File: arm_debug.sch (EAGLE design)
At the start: 14 parts, among them P1 FTSH-105-01-L-DV-K-TR, P2 FTSH-105-01-L-DV-K-TR, P3 MOLEX_MICRO_USB, P4 MEC6-110-02-L-D-RA1, U1 FT234XD-T

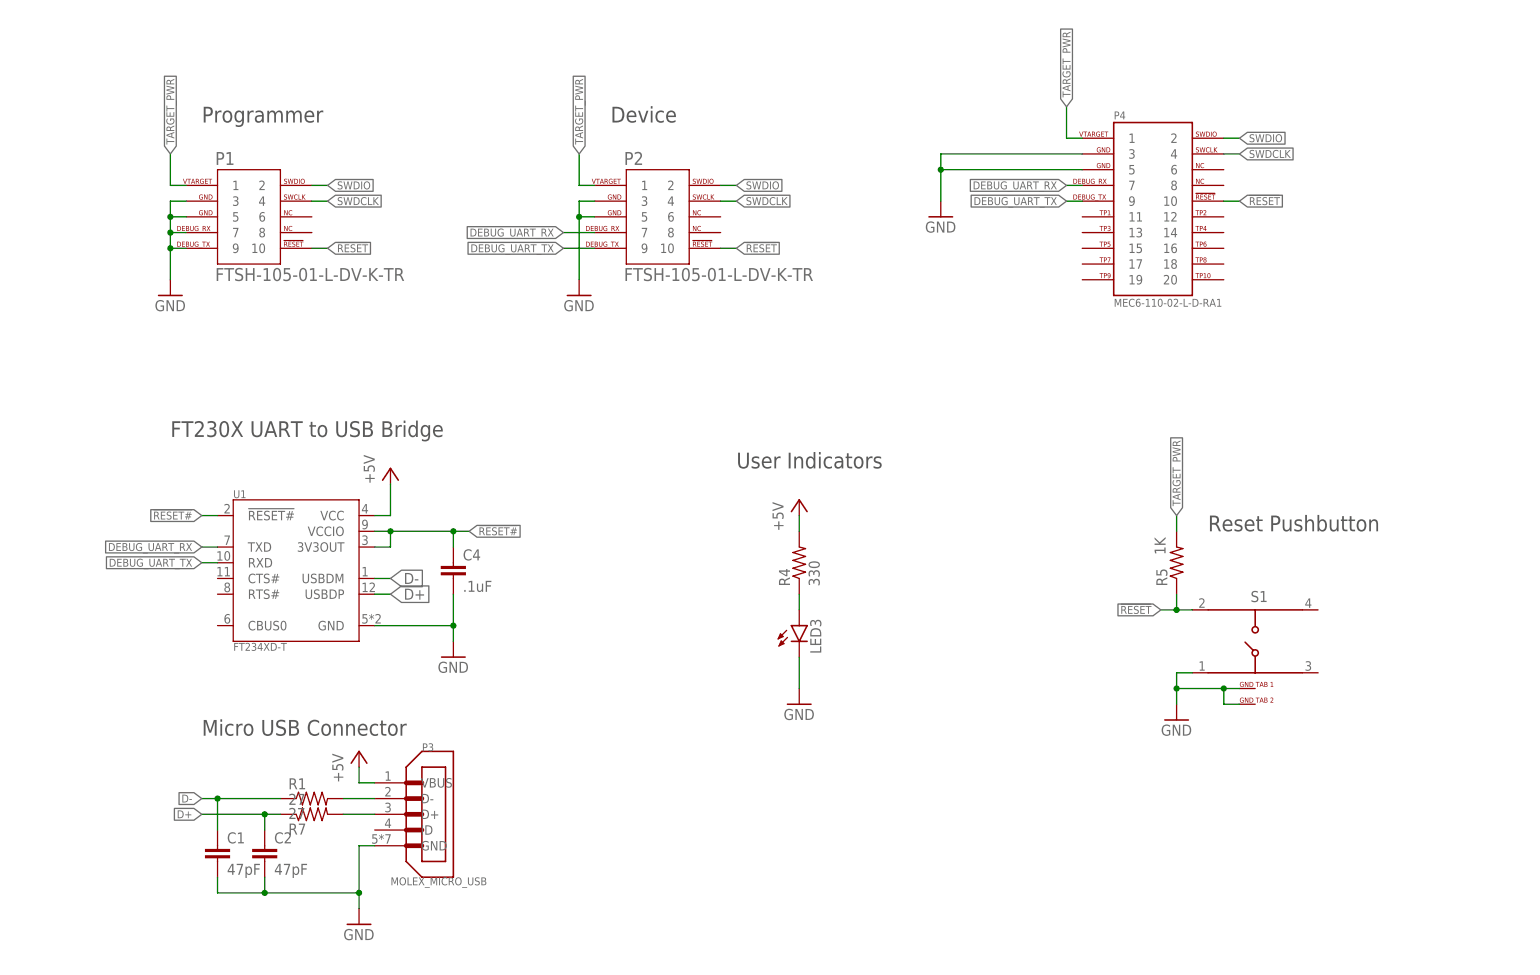
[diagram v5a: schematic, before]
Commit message: Seperating passive components into individual managed libraries
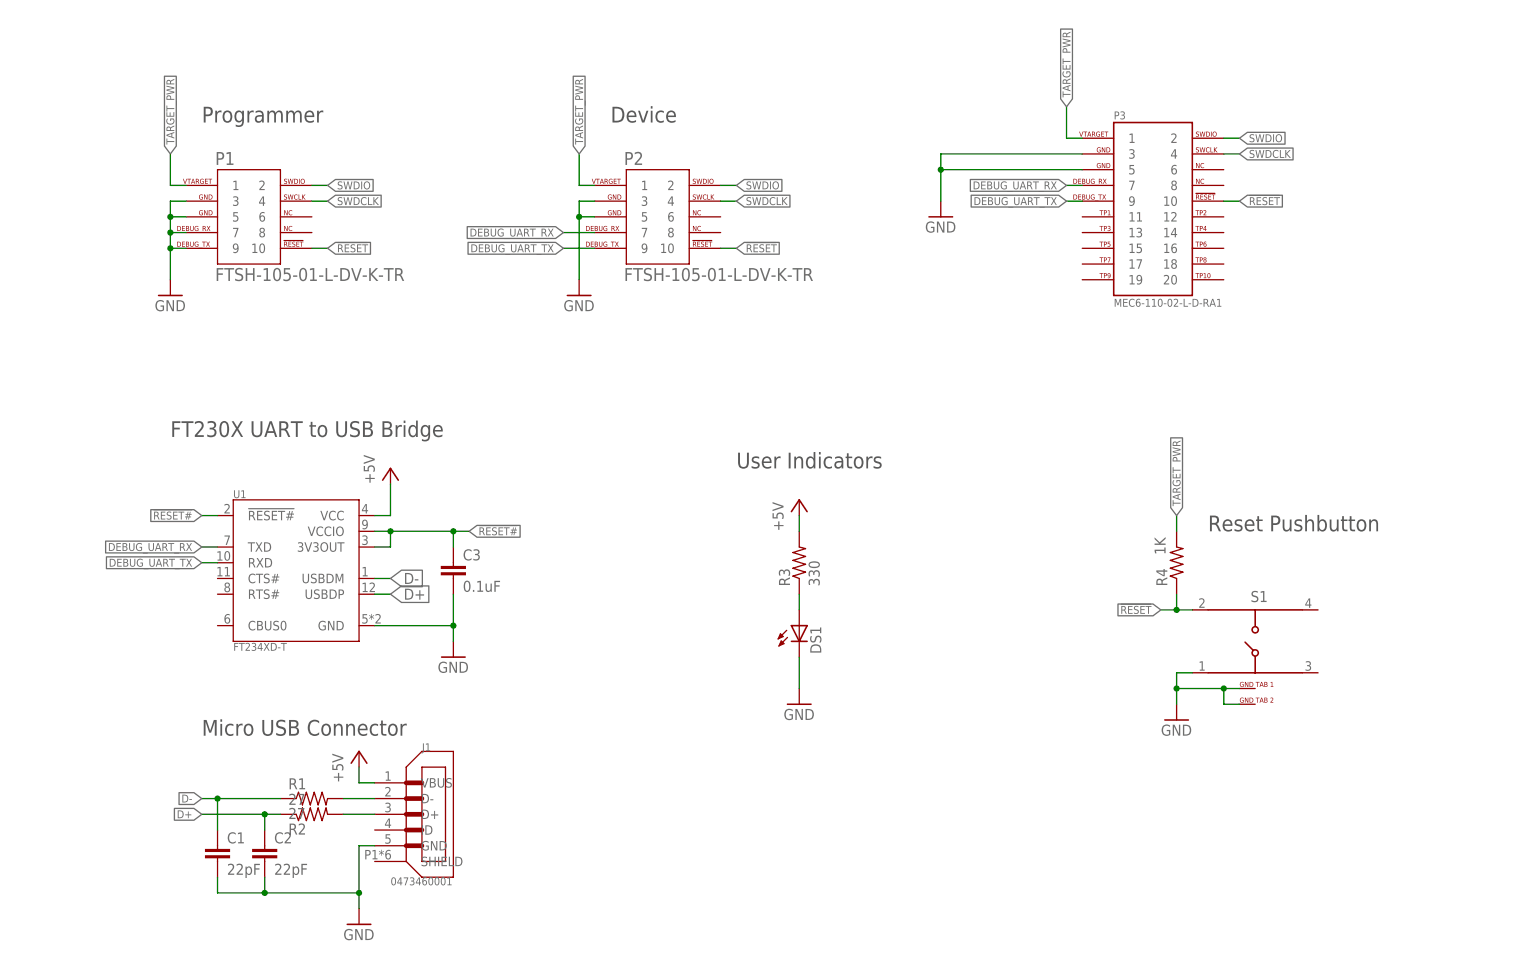
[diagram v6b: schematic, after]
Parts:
- removed C4: .1uF, resistor:C-EUC0603
- removed LED3: (no value), led:LEDCHIPLED_0603
- removed P4: MEC6-110-02-L-D-RA1, programming_headers:SWD-MEC10-F
- removed R5: 1K, resistor:R-US_R0603
- removed R7: 27, resistor:R-US_R0603
- added C3: 0.1uF, capacitors:0603YC104KAT2A
- added DS1: (no value), leds:LED0603
- added J1: 0473460001, board_connectivity:MOLEX_MICRO_USB
- added R2: 27, resistors:ESR03EZPJ270-27
- added R3: 330, resistors:RR0816P-331-D
- C1, C2: value 47pF -> 22pF; device resistor:C-EUC0603 -> capacitors:C0603C220M4RACAUTO
- P3: value MOLEX_MICRO_USB -> MEC6-110-02-L-D-RA1; device board_connectivity:MOLEX_MICRO_USB -> programming_headers:SWD-MEC10-F
- R1: device resistor:R-US_R0603 -> resistors:ESR03EZPJ270-27
- R4: value 330 -> 1K; device resistor:R-US_R0603 -> resistors:RR0816P-102-D
- S1: value WURTH_SMD_PB -> 431181015816; device switches:WURTH_SMD_PB -> switches:431181015816
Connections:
- net !RESET: now also P3.10, R4.1; no longer P4.10, R5.1
- net !RESET#: now also C3.1; no longer C4.1
- net +5V: now also J1.VBUS, R3.2; no longer P3.VBUS, R4.2
- net D+: now also R2.1; no longer R7.1
- net DEBUG_UART_RX: now also P3.7; no longer P4.7
- net DEBUG_UART_TX: now also P3.9; no longer P4.9
- net GND: now also C3.2, DS1.C, J1.GND, P3.3, P3.5; no longer C4.2, LED3.C, P3.GND, P4.3, P4.5
- net N$2: now also J1.D-; no longer P3.D-
- net N$3: now also DS1.A, R3.1; no longer LED3.A, R4.1
- net N$4: now also J1.D+, R2.2; no longer P3.D+, R7.2
- net SWDCLK: now also P3.4; no longer P4.4
- net SWDIO: now also P3.2; no longer P4.2
- net TARGET_PWR: now also P3.1, R4.2; no longer P4.1, R5.2
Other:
- moved on the sheet: R4
